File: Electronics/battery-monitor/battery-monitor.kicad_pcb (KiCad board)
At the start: 2 copper layers, 2 parts, among them U1 ACS714LLCTR-30A-T, U2 ACS714LLCTR-30A-T

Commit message: base layout done, freeroute files exported
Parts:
- added C1: C, Capacitors_THT:C_Rect_L4.6mm_W3.8mm_P2.50mm_MKS02_FKP02, F.Cu at (101.6, 76.2)
- added C2: C, Capacitors_THT:C_Rect_L4.6mm_W3.8mm_P2.50mm_MKS02_FKP02, F.Cu at (101.6, 67.3)
- added J1: Screw_Terminal_1x02, Connectors_Terminal_Blocks:TerminalBlock_Pheonix_PT-3.5mm_2pol, F.Cu at (71.1, 73.7)
- added J2: Screw_Terminal_1x02, Connectors_Terminal_Blocks:TerminalBlock_Pheonix_PT-3.5mm_2pol, F.Cu at (71.1, 66.0)
- added J3: Screw_Terminal_1x06, Connectors_Terminal_Blocks:TerminalBlock_Pheonix_PT-3.5mm_6pol, F.Cu at (111.8, 63.5)
- added R1: R, Resistors_THT:R_Axial_DIN0207_L6.3mm_D2.5mm_P7.62mm_Horizontal, F.Cu at (78.7, 77.5)
- added R2: R, Resistors_THT:R_Axial_DIN0207_L6.3mm_D2.5mm_P7.62mm_Horizontal, F.Cu at (78.7, 73.7)
- added R3: R, Resistors_THT:R_Axial_DIN0207_L6.3mm_D2.5mm_P7.62mm_Horizontal, F.Cu at (78.7, 69.8)
- added R4: R, Resistors_THT:R_Axial_DIN0207_L6.3mm_D2.5mm_P7.62mm_Horizontal, F.Cu at (78.7, 66.0)
- moved U2 66.3 mm to (94.0, 67.3), turned to 270 degrees
- moved U1 61.7 mm to (94.0, 76.2), turned to 270 degrees
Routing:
- net GND: track 0.00 -> 9.33 mm
- net Net-(J2-Pad1): track 0.00 -> 9.20 mm
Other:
- board outline added: 53.3 x 30.5 mm

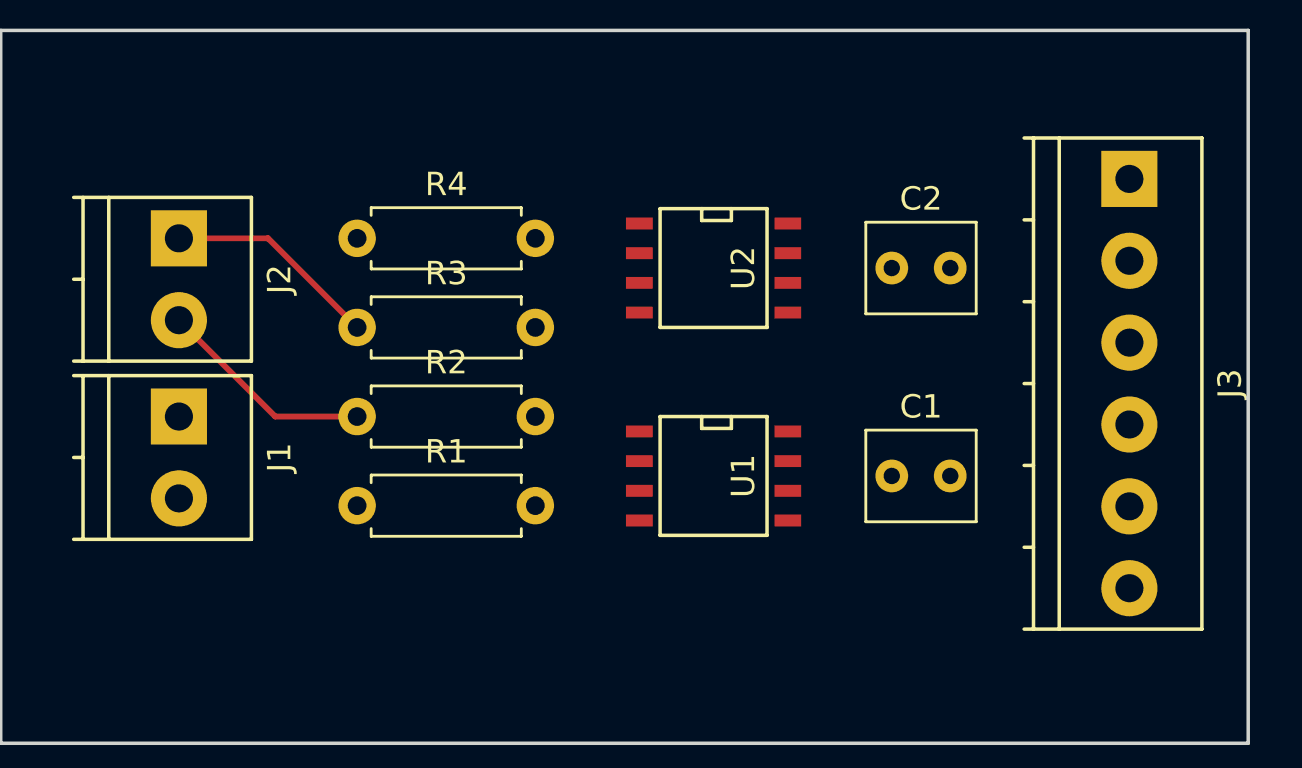
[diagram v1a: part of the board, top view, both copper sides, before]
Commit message: svg created, fighting with various cam software to get my process down
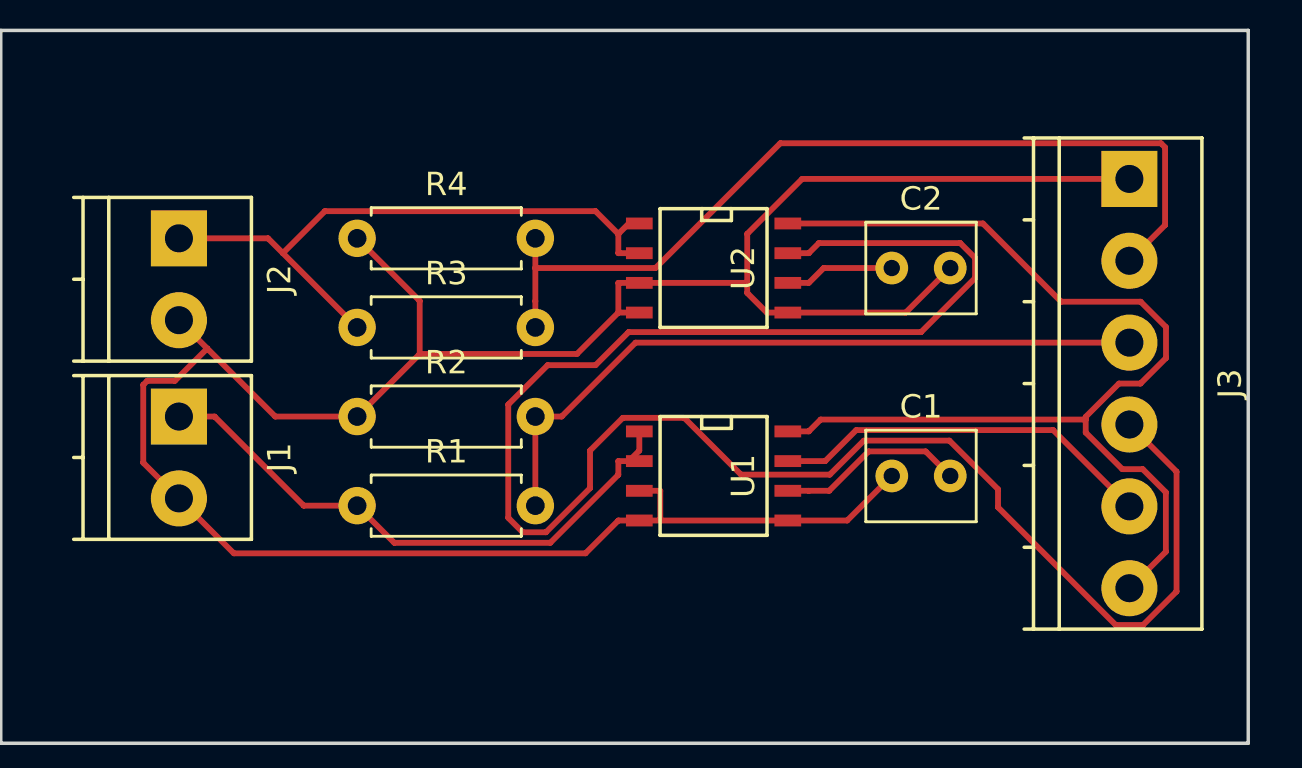
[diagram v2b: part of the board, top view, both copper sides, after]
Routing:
- net GND: track 9.33 -> 109.6 mm
- net Net-(J3-Pad4): track 0.00 -> 82.0 mm
- net Net-(J3-Pad6): track 0.00 -> 46.7 mm
- net Net-(J3-Pad2): track 0.00 -> 38.5 mm
- net Net-(J3-Pad3): track 0.00 -> 30.5 mm
- net Net-(J1-Pad1): track 0.00 -> 25.2 mm
- net Net-(J2-Pad1): track 9.20 -> 27.5 mm
- net Net-(J3-Pad5): track 0.00 -> 16.5 mm
- net Net-(C1-Pad2): track 0.00 -> 8.08 mm
- net Net-(C2-Pad1): track 0.00 -> 4.71 mm

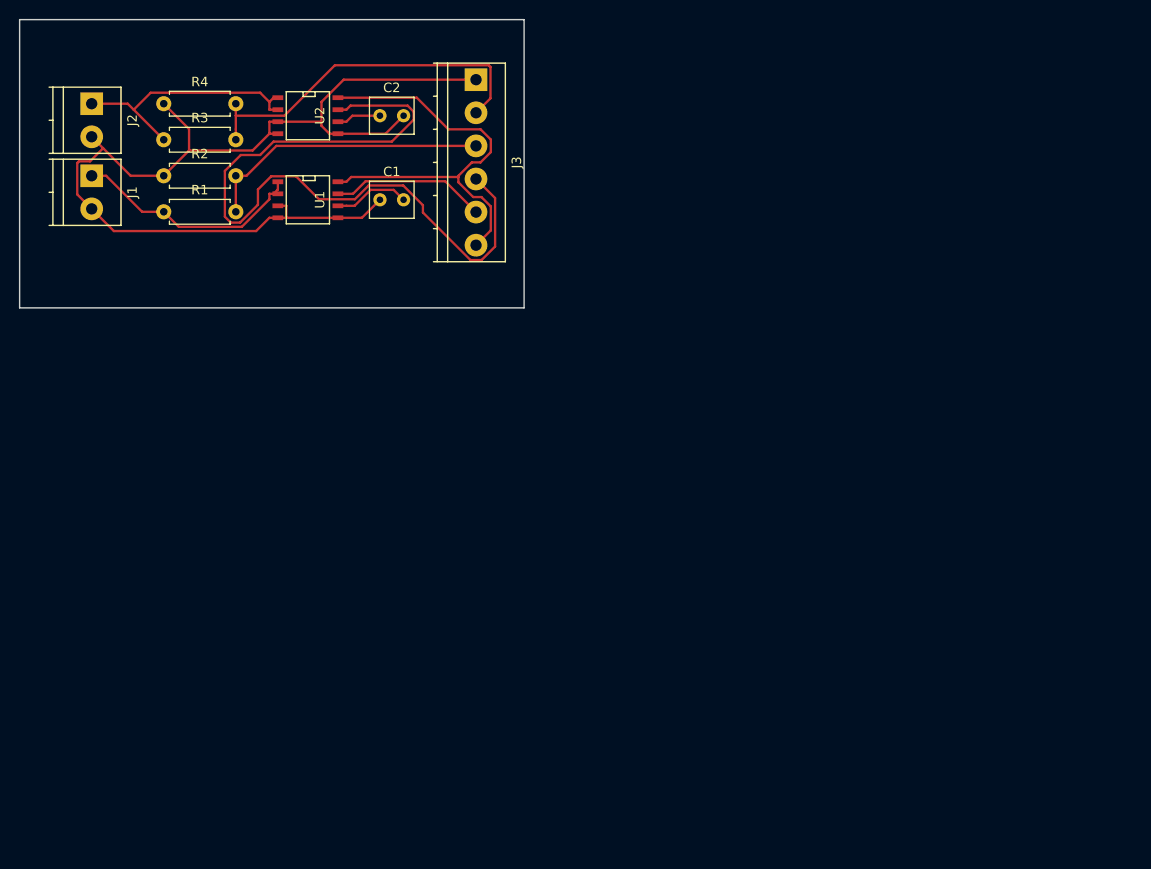
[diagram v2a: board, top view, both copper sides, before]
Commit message: board changed to add ATMEGA for onboard monitoring
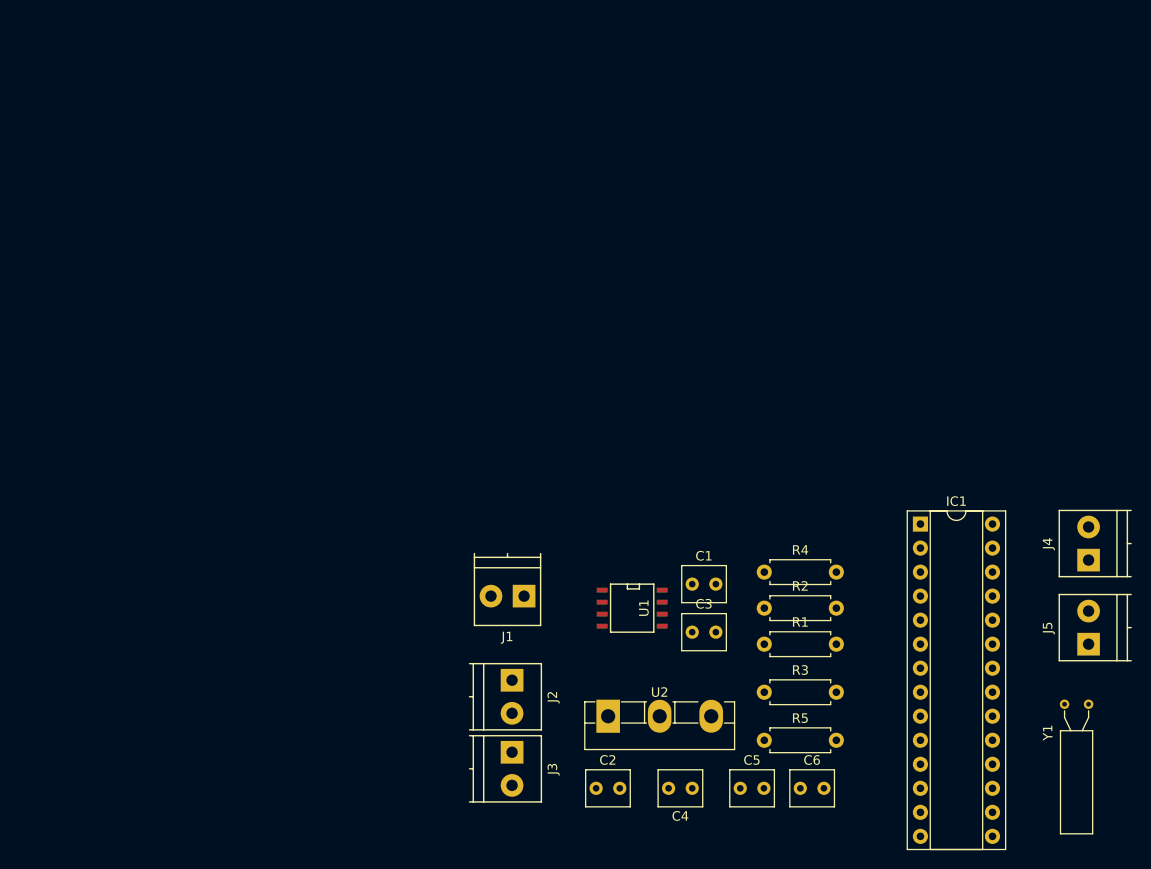
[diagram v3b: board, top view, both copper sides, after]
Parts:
- added C3: C, Capacitors_THT:C_Rect_L4.6mm_W3.8mm_P2.50mm_MKS02_FKP02, F.Cu at (134.6, 121.9)
- added C4: C, Capacitors_THT:C_Rect_L4.6mm_W3.8mm_P2.50mm_MKS02_FKP02, F.Cu at (134.6, 138.4)
- added C5: C, Capacitors_THT:C_Rect_L4.6mm_W3.8mm_P2.50mm_MKS02_FKP02, F.Cu at (139.7, 138.4)
- added C6: C, Capacitors_THT:C_Rect_L4.6mm_W3.8mm_P2.50mm_MKS02_FKP02, F.Cu at (146.1, 138.4)
- added IC1: ATMEGA328P-P, Housings_DIP:DIP-28_W7.62mm_Socket, F.Cu at (158.8, 110.5)
- added J4: Screw_Terminal_1x02, Connectors_Terminal_Blocks:TerminalBlock_Pheonix_PT-3.5mm_2pol, F.Cu at (176.5, 114.3)
- added J5: Screw_Terminal_1x02, Connectors_Terminal_Blocks:TerminalBlock_Pheonix_PT-3.5mm_2pol, F.Cu at (176.5, 123.2)
- added R5: R, Resistors_THT:R_Axial_DIN0207_L6.3mm_D2.5mm_P7.62mm_Horizontal, F.Cu at (142.2, 133.3)
- added Y1: Crystal, Crystals:Crystal_AT310_d3.0mm_l10.0mm_Horizontal, F.Cu at (174.0, 129.5)
- J3: value Screw_Terminal_1x06 -> Screw_Terminal_1x02; footprint Connectors_Terminal_Blocks:TerminalBlock_Pheonix_PT-3.5mm_6pol -> Connectors_Terminal_Blocks:TerminalBlock_Pheonix_PT-3.5mm_2pol
- U2: value ACS714LLCTR-30A-T -> LM7805CT; footprint SMD_Packages:SOIC-8-N -> TO_SOT_Packages_THT:TO-3PB__Vertical
- moved R3 86.3 mm to (142.2, 128.3)
- moved R4 80.5 mm to (142.2, 115.6)
- moved R1 78.2 mm to (142.2, 123.2)
- moved R2 78.2 mm to (142.2, 119.4)
- moved J2 75.4 mm to (115.6, 127.0)
- moved C2 74.7 mm to (124.5, 138.4)
- moved J3 71.2 mm to (115.6, 134.6)
- moved U2 71.0 mm to (125.7, 130.8), turned to 0 degrees
- moved J1 63.8 mm to (116.8, 118.1), turned to 180 degrees
- moved U1 55.1 mm to (128.3, 119.4)
- moved C1 52.4 mm to (134.6, 116.8)
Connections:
- C1 pad 1: GND -> Net-(C1-Pad1)
- C2 pad 2: GND -> Net-(C1-Pad1)
- J1 pad 1: Net-(J1-Pad1) -> Net-(C2-Pad1)
- J1 pad 2: GND -> Net-(C1-Pad1)
- J2 pad 1: Net-(J2-Pad1) -> Net-(C2-Pad1)
- J2 pad 2: GND -> Net-(C1-Pad1)
- J3 pad 1: GND -> Net-(C2-Pad1)
- J3 pad 2: Net-(J3-Pad2) -> Net-(C1-Pad1)
- R1 pad 1: Net-(J1-Pad1) -> Net-(C2-Pad1)
- R1 pad 2: Net-(J3-Pad3) -> Net-(IC1-Pad24)
- R2 pad 1: GND -> Net-(C1-Pad1)
- R2 pad 2: Net-(J3-Pad3) -> Net-(IC1-Pad24)
- R3 pad 1: Net-(J2-Pad1) -> Net-(C2-Pad1)
- R3 pad 2: Net-(J3-Pad2) -> Net-(IC1-Pad23)
- R4 pad 1: GND -> Net-(C1-Pad1)
- R4 pad 2: Net-(J3-Pad2) -> Net-(IC1-Pad23)
- U1 pad 1: Net-(J1-Pad1) -> Net-(C2-Pad1)
- U1 pad 2: Net-(J1-Pad1) -> Net-(C2-Pad1)
- U1 pad 3: GND -> Net-(C1-Pad1)
- U1 pad 4: GND -> Net-(C1-Pad1)
- U1 pad 5: GND -> Net-(C1-Pad1)
- U1 pad 7: Net-(J3-Pad5) -> Net-(IC1-Pad25)
- U1 pad 8: Net-(J3-Pad6) -> Net-(C3-Pad1)
- U2 pad 1: Net-(J2-Pad1) -> Net-(C2-Pad1)
- U2 pad 2: Net-(J2-Pad1) -> Net-(C1-Pad1)
- U2 pad 3: GND -> Net-(C3-Pad1)
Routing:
- net GND: track 109.6 -> 0.00 mm
- net Net-(J3-Pad4): track 82.0 -> 0.00 mm
- net Net-(J3-Pad6): track 46.7 -> 0.00 mm
- net Net-(J3-Pad2): track 38.5 -> 0.00 mm
- net Net-(J3-Pad3): track 30.5 -> 0.00 mm
- net Net-(J2-Pad1): track 27.5 -> 0.00 mm
- net Net-(J1-Pad1): track 25.2 -> 0.00 mm
- net Net-(J3-Pad5): track 16.5 -> 0.00 mm
- net Net-(C1-Pad2): track 8.08 -> 0.00 mm
- net Net-(C2-Pad1): track 4.71 -> 0.00 mm
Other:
- board outline removed
- rule pad_to_mask_clearance: 0.2 -> 0
